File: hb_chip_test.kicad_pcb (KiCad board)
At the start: 2 copper layers, 174 parts, among them J1 31-5431-2010_CID2.5.196, J13 2x8, J2 31-5431-2010_CID2.5.196, J3 31-5431-2010_CID2.5.196, J4 1945193_12P_CID2.2.928, J5 31-5431-2010_CID2.5.196, J6 31-5431-2010_CID2.5.196, J7 31-5431-2010_CID2.5.196, J8 2x8, U1 L7812ABD2T-TR_CID8.52.934, U2 MC7912ACD2TR4G_CID8.52.429, U3 LP2981IM5-5.0-NOPB_CID8.52.176, U5 TL084, U6 MCP3202, U7 REF5050ID, U8 Tang_Nano_9K, U9 TL082

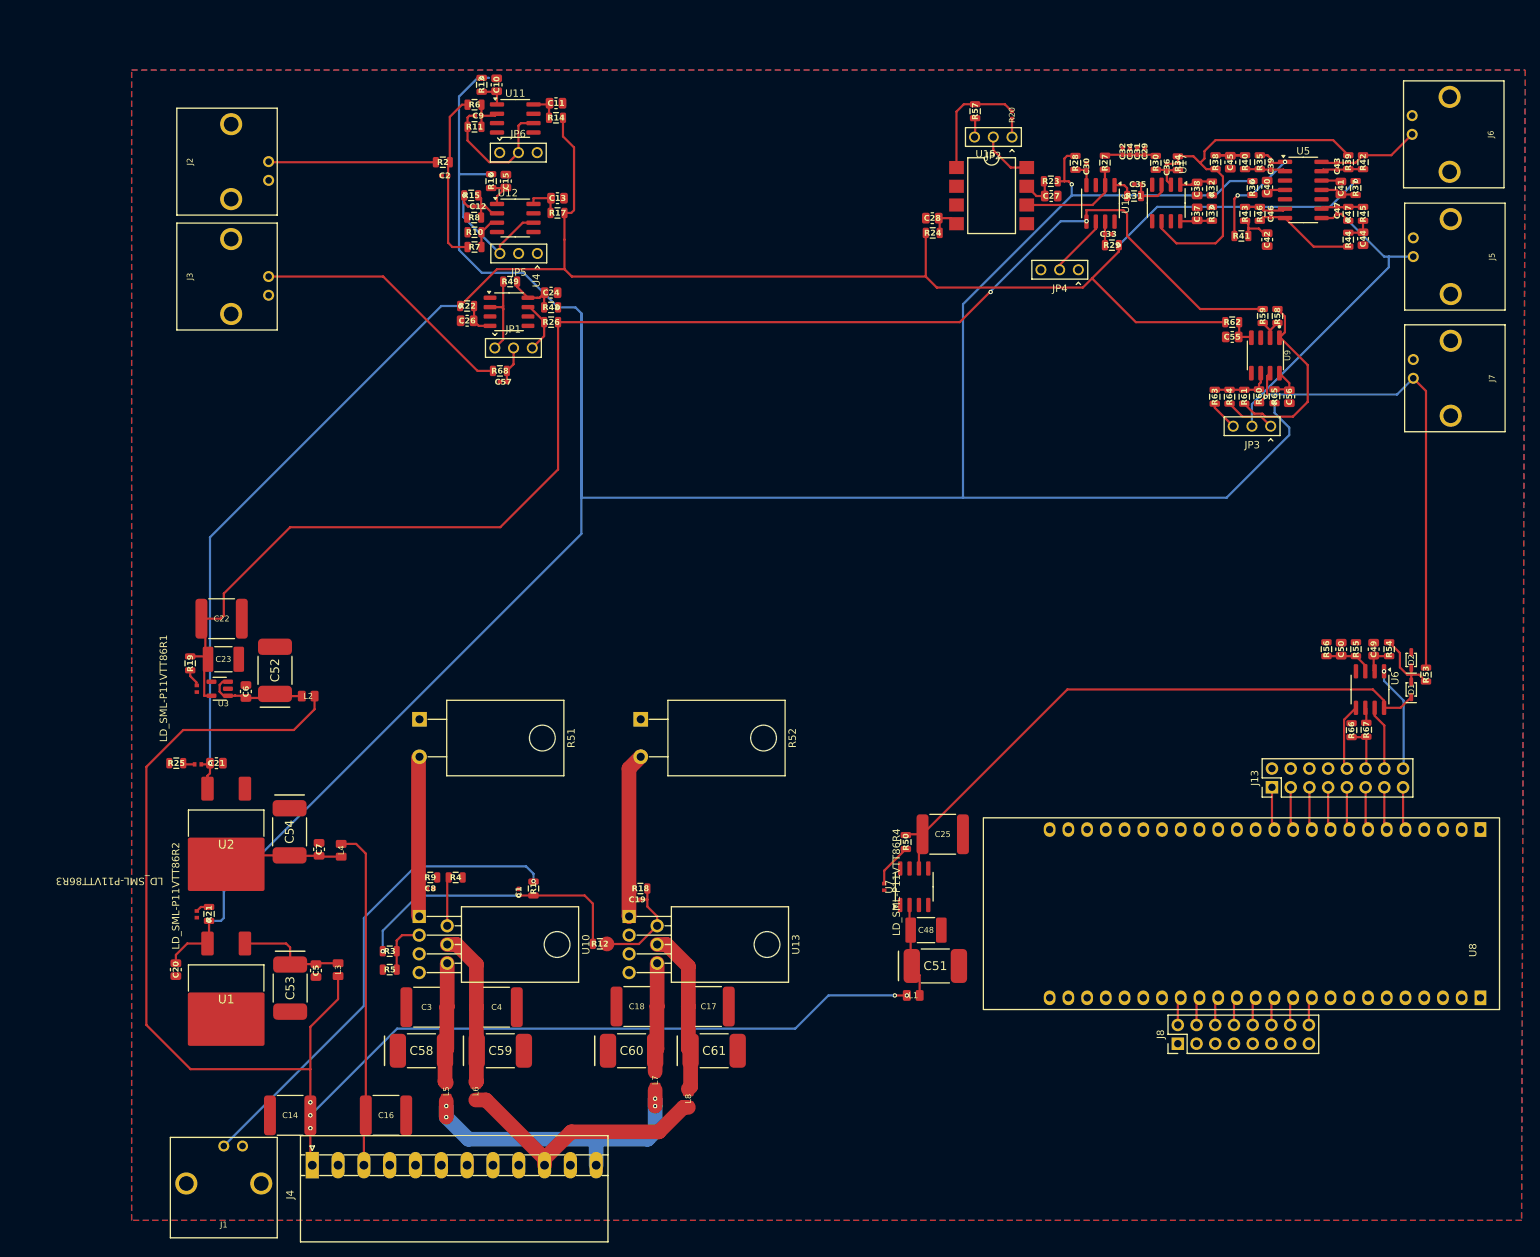
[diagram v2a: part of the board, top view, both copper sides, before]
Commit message: PCBv2
Room for heatsinks, wiring corrections.
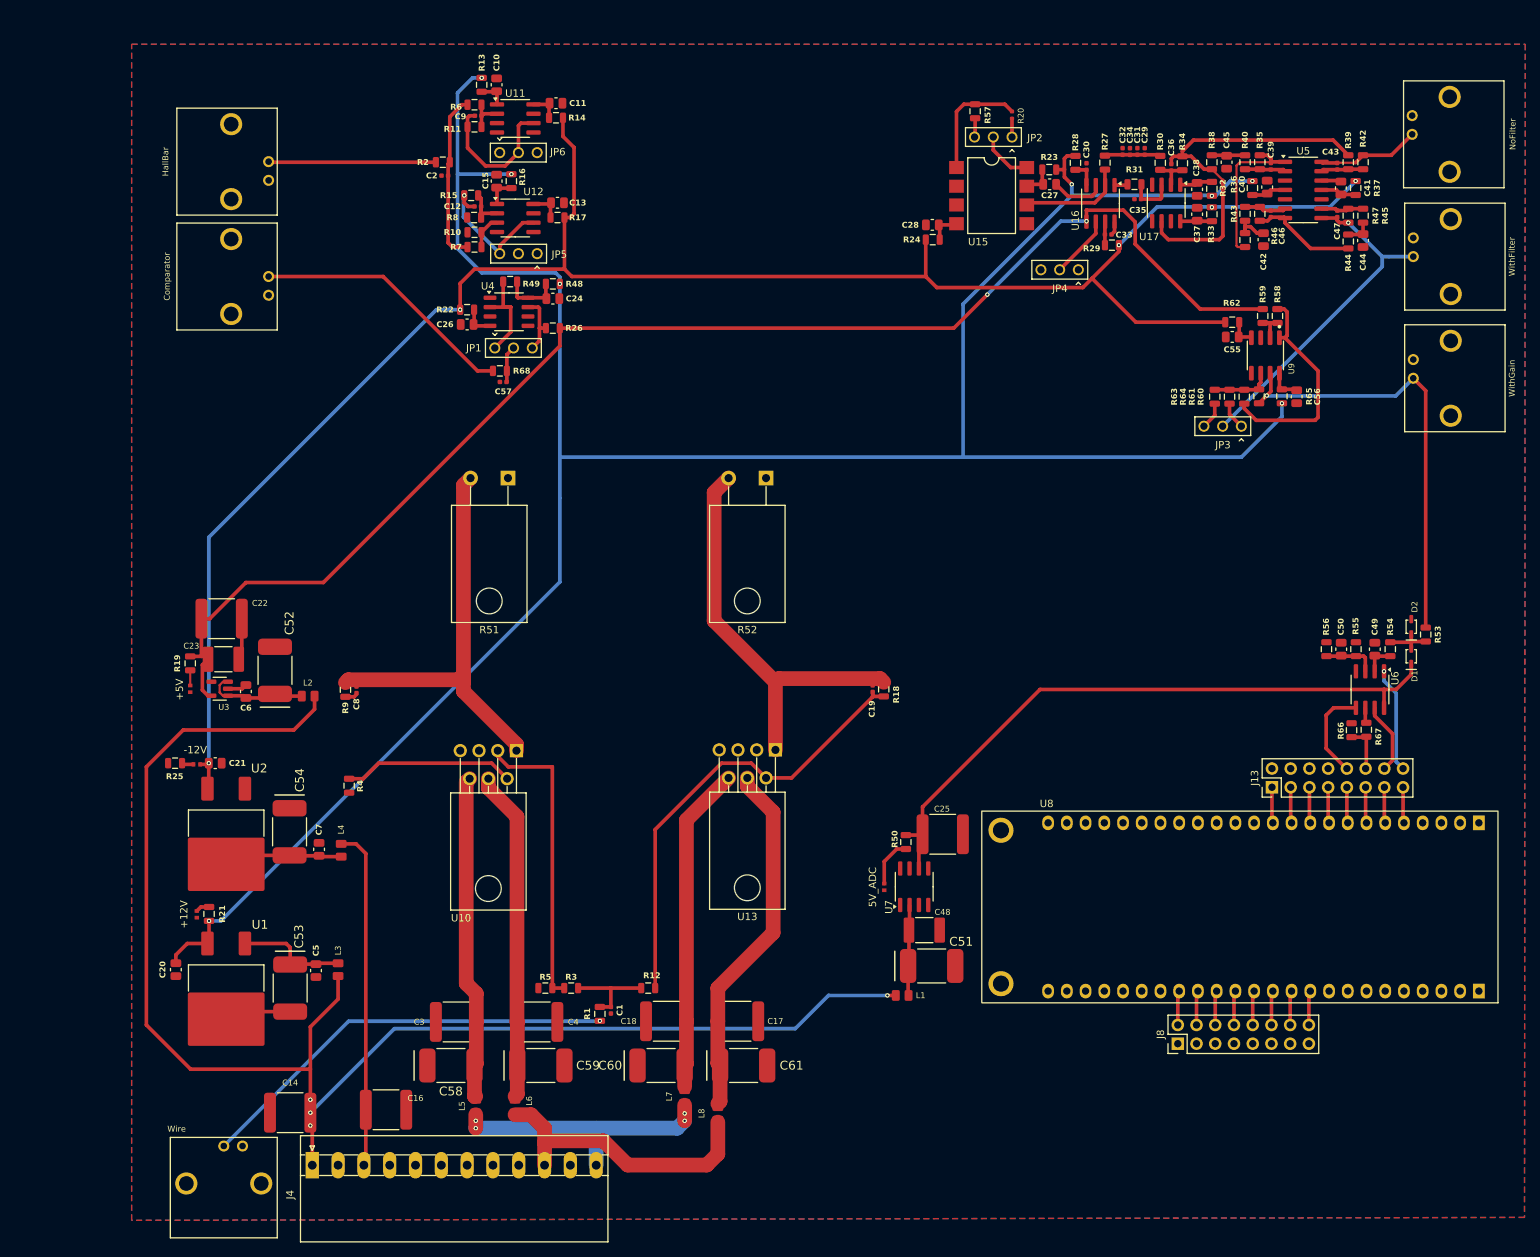
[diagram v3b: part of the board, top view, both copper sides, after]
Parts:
- moved C19 42.9 mm to (162.5, 107.9), turned to 90 degrees
- moved R18 42.6 mm to (164.0, 108.0), turned to 90 degrees
- moved R52 36.9 mm to (148.0, 79.3), turned to 180 degrees
- moved R51 34.8 mm to (113.0, 79.3), turned to 180 degrees
- moved U13 30.1 mm to (149.3, 116.2), turned to 180 degrees
- moved C8 28.7 mm to (92.5, 108.1), turned to 90 degrees
- moved R9 27.9 mm to (91.0, 108.1), turned to 90 degrees
- moved U10 26.1 mm to (114.2, 116.3), turned to 180 degrees
- moved R3 25.1 mm to (121.6, 148.5), turned to 180 degrees
- moved R5 21.3 mm to (118.1, 148.5)
- moved C1 20.3 mm to (127.0, 151.5), turned to 90 degrees
- moved R1 19.2 mm to (125.5, 152.0), turned to 90 degrees
- moved R4 19.1 mm to (91.5, 121.1), turned to 90 degrees
- moved R12 8.89 mm to (132.1, 148.5)
- moved C4 5.85 mm to (117.0, 153.1)
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- renumbered LD_SML-P11VTT86R2 to +12V, LD_SML-P11VTT86R1 to +5V, LD_SML-P11VTT86R3 to -12V, LD_SML-P11VTT86R4 to 5V_ADC, J3 to Comparator, J2 to HallBar, J6 to NoFilter, J1 to Wire, J5 to WithFilter, J7 to WithGain
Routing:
- net Net-(U13--): track 14.3 -> 62.1 mm
- net Net-(U10-+): track 7.36 -> 40.4 mm
- net Net-(U10-Vo): track 24.9 -> 57.8 mm
- net +12V: track 375.0 -> 342.3 mm
- net Net-(U13-V-): track 14.8 -> 44.3 mm
- net Net-(U13-Vo): track 27.3 -> 56.2 mm
- net GND: track 2.69 -> 31.1 mm
- net Net-(U10-V-): track 16.4 -> 44.1 mm
- net Net-(C1-Pad2): track 39.5 -> 12.6 mm, vias 2 -> 0
- net Net-(U13-V+): track 22.3 -> 49.0 mm
- net Net-(U10-V+): track 21.1 -> 44.8 mm
- net Net-(U10--): track 6.63 -> 23.2 mm
- net +5V: track 203.2 -> 190.3 mm
- net Net-(J1-Pad1): track 66.1 -> 58.0 mm
- net Net-(J7-Pad1): track 67.0 -> 60.2 mm
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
